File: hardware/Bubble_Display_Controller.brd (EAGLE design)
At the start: 38.1 x 43.2 mm, 37 parts, among them J1 ICSP, Q1 BSS84, Q10 BSS123, Q11 BSS123, Q12 BSS123, Q13 BSS123, Q14 BSS123, Q15 BSS123, Q16 BSS123, Q2 BSS84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

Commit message: Updating comp values per simulation. Added BOM. Started firmware.
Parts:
- C1: value 0.1u -> 0.1uF
- C3: value CAP_POL0805 -> 10uF
- Q10, Q11, Q12, Q13, Q14, Q15, Q16, Q9: value BSS123 -> IRFML8244
- R1, R2, R3, R4, R5, R6, R7, R8: value 180 -> 75
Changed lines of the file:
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@@
 <element name="DISPLAY2" library="SparkFun-Displays" package="DIL12" value="hp" x="11.43" y="29.21" rot="MR0"/>
 <element name="Q1" library="SparkFun-DiscreteSemi" package="SOT23-3" value="BSS84" x="33.02" y="39.37" rot="R180"/>
-<element name="R1" library="SparkFun-Resistors" package="0805" value="180" x="33.02" y="35.56"/>
+<element name="R1" library="SparkFun-Resistors" package="0805" value="75" x="33.02" y="35.56"/>
 <element name="Q2" library="SparkFun-DiscreteSemi" package="SOT23-3" value="BSS84" x="16.51" y="39.37" rot="R180"/>
-<element name="R2" library="SparkFun-Resistors" package="0805" value="180" x="15.24" y="35.56"/>
+<element name="R2" library="SparkFun-Resistors" package="0805" value="75" x="15.24" y="35.56"/>
 <element name="Q3" library="SparkFun-DiscreteSemi" package="SOT23-3" value="BSS84" x="30.48" y="19.05"/>
-<element name="R3" library="SparkFun-Resistors" package="0805" value="180" x="30.48" y="22.86"/>
+<element name="R3" library="SparkFun-Resistors" package="0805" value="75" x="30.48" y="22.86"/>
 <element name="Q4" library="SparkFun-DiscreteSemi" package="SOT23-3" value="BSS84" x="22.86" y="39.37" rot="R180"/>
-<element name="R4" library="SparkFun-Resistors" package="0805" value="180" x="22.86" y="35.56"/>
+<element name="R4" library="SparkFun-Resistors" package="0805" value="75" x="22.86" y="35.56"/>
 <element name="Q5" library="SparkFun-DiscreteSemi" package="SOT23-3" value="BSS84" x="15.24" y="19.05"/>
-<element name="R5" library="SparkFun-Resistors" package="0805" value="180" x="15.24" y="22.86"/>
+<element name="R5" library="SparkFun-Resistors" package="0805" value="75" x="15.24" y="22.86"/>
 <element name="Q6" library="SparkFun-DiscreteSemi" package="SOT23-3" value="BSS84" x="8.89" y="39.37" rot="R180"/>
-<element name="R6" library="SparkFun-Resistors" package="0805" value="180" x="10.16" y="35.56" rot="R180"/>
+<element name="R6" library="SparkFun-Resistors" package="0805" value="75" x="10.16" y="35.56" rot="R180"/>
 <element name="Q7" library="SparkFun-DiscreteSemi" package="SOT23-3" value="BSS84" x="5.08" y="39.37" rot="R180"/>
-<element name="R7" library="SparkFun-Resistors" package="0805" value="180" x="5.08" y="35.56"/>
+<element name="R7" library="SparkFun-Resistors" package="0805" value="75" x="5.08" y="35.56"/>
 <element name="Q8" library="SparkFun-DiscreteSemi" package="SOT23-3" value="BSS84" x="7.62" y="19.05"/>
-<element name="R8" library="SparkFun-Resistors" package="0805" value="180" x="7.62" y="22.86"/>
-<element name="C3" library="ChipsParts" package="0805-POL" value="CAP_POL0805" x="5.08" y="6.985" rot="R270"/>
-<element name="C1" library="SparkFun-Capacitors" package="0805" value="0.1u" x="16.51" y="1.905" rot="R180"/>
+<element name="R8" library="SparkFun-Resistors" package="0805" value="75" x="7.62" y="22.86"/>
+<element name="C3" library="ChipsParts" package="0805-POL" value="10uF" x="5.08" y="6.985" rot="R270"/>
+<element name="C1" library="SparkFun-Capacitors" package="0805" value="0.1uF" x="16.51" y="1.905" rot="R180"/>
 <element name="J1" library="SparkFun" package="2X3" value="ICSP" x="36.195" y="3.175" rot="R90"/>
 <element name="C5" library="SparkFun-Capacitors" package="0805" value="0.1uF" x="20.955" y="1.905"/>
@@
 <element name="Y1" library="SparkFun-FreqCtrl" package="RESONATOR-SMD" value="16MHz" x="16.51" y="15.24" rot="R180"/>
 <element name="JP1" library="SparkFun-Connectors" package="1X04" value="I2C" x="1.905" y="2.54"/>
-<element name="Q9" library="SparkFun-DiscreteSemi" package="SOT23" value="BSS123" x="34.29" y="21.59">
+<element name="Q9" library="SparkFun-DiscreteSemi" package="SOT23" value="IRFML8244" x="34.29" y="21.59">
 <attribute name="PROD_ID" value="TRANS-08345" x="69.85" y="-16.51" size="1.778" layer="27" display="off"/>
 </element>
-<element name="Q10" library="SparkFun-DiscreteSemi" package="SOT23" value="BSS123" x="27.94" y="38.1" rot="R180">
+<element name="Q10" library="SparkFun-DiscreteSemi" package="SOT23" value="IRFML8244" x="27.94" y="38.1" rot="R180">
 <attribute name="PROD_ID" value="TRANS-08345" x="-11.43" y="76.2" size="1.778" layer="27" rot="R180" display="off"/>
 </element>
-<element name="Q11" library="SparkFun-DiscreteSemi" package="SOT23" value="BSS123" x="26.67" y="21.59">
+<element name="Q11" library="SparkFun-DiscreteSemi" package="SOT23" value="IRFML8244" x="26.67" y="21.59">
 <attribute name="PROD_ID" value="TRANS-08345" x="69.85" y="-16.51" size="1.778" layer="27" display="off"/>
 </element>
-<element name="Q12" library="SparkFun-DiscreteSemi" package="SOT23" value="BSS123" x="22.86" y="21.59">
+<element name="Q12" library="SparkFun-DiscreteSemi" package="SOT23" value="IRFML8244" x="22.86" y="21.59">
 <attribute name="PROD_ID" value="TRANS-08345" x="69.85" y="-16.51" size="1.778" layer="27" display="off"/>
 </element>
-<element name="Q13" library="SparkFun-DiscreteSemi" package="SOT23" value="BSS123" x="3.81" y="21.59">
+<element name="Q13" library="SparkFun-DiscreteSemi" package="SOT23" value="IRFML8244" x="3.81" y="21.59">
 <attribute name="PROD_ID" value="TRANS-08345" x="54.61" y="-16.51" size="1.778" layer="27" display="off"/>
 </element>
-<element name="Q14" library="SparkFun-DiscreteSemi" package="SOT23" value="BSS123" x="11.43" y="21.59">
+<element name="Q14" library="SparkFun-DiscreteSemi" package="SOT23" value="IRFML8244" x="11.43" y="21.59">
 <attribute name="PROD_ID" value="TRANS-08345" x="66.04" y="-16.51" size="1.778" layer="27" display="off"/>
 </element>
-<element name="Q15" library="SparkFun-DiscreteSemi" package="SOT23" value="BSS123" x="12.7" y="38.1" rot="R180">
+<element name="Q15" library="SparkFun-DiscreteSemi" package="SOT23" value="IRFML8244" x="12.7" y="38.1" rot="R180">
 <attribute name="PROD_ID" value="TRANS-08345" x="-2.54" y="87.63" size="1.778" layer="27" rot="R180" display="off"/>
 </element>
-<element name="Q16" library="SparkFun-DiscreteSemi" package="SOT23" value="BSS123" x="19.05" y="21.59">
+<element name="Q16" library="SparkFun-DiscreteSemi" package="SOT23" value="IRFML8244" x="19.05" y="21.59">
 <attribute name="PROD_ID" value="TRANS-08345" x="38.1" y="-27.94" size="1.778" layer="27" display="off"/>
 </element>

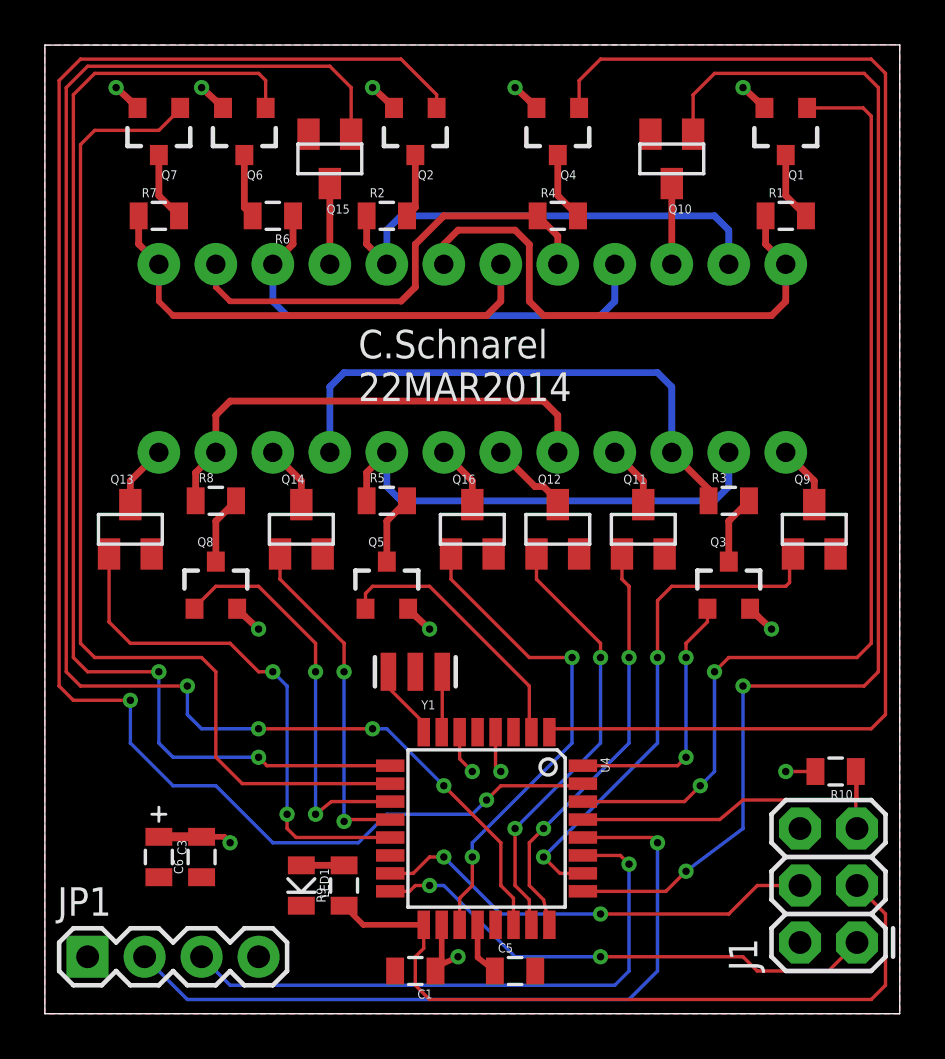
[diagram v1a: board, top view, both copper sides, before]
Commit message: Updated to use new HP Display component in my fork of SparkFun libraries
Also worked on CharGenROM.h; converted segments to HP config.  Added
proper port manipulation to Display_Firmware.ino.
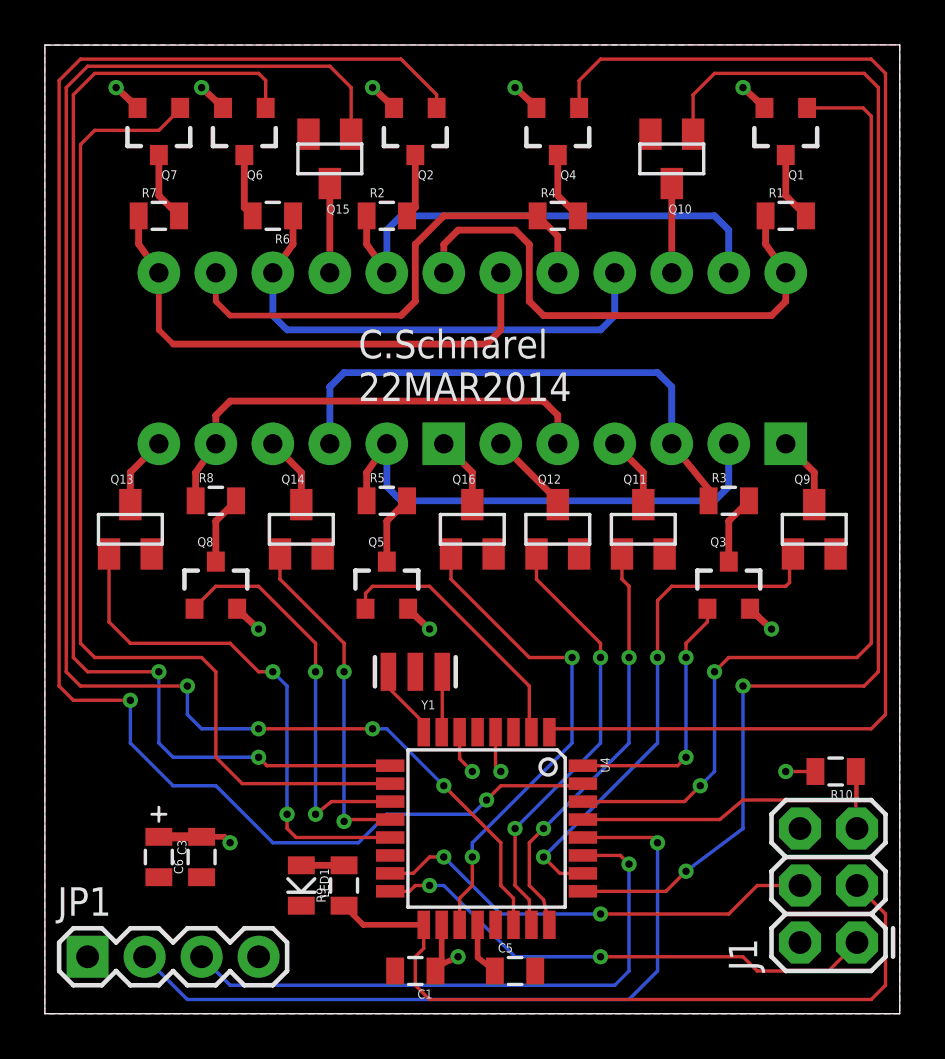
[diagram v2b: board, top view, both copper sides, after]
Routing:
- net SEGG: track 21.6 -> 23.7 mm
- net SEGD: track 20.8 -> 22.1 mm
- net SEGE: track 21.3 -> 22.4 mm
- net SEGB: track 21.3 -> 22.4 mm
- net SEGF: track 21.6 -> 22.4 mm

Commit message: Some signal name changes
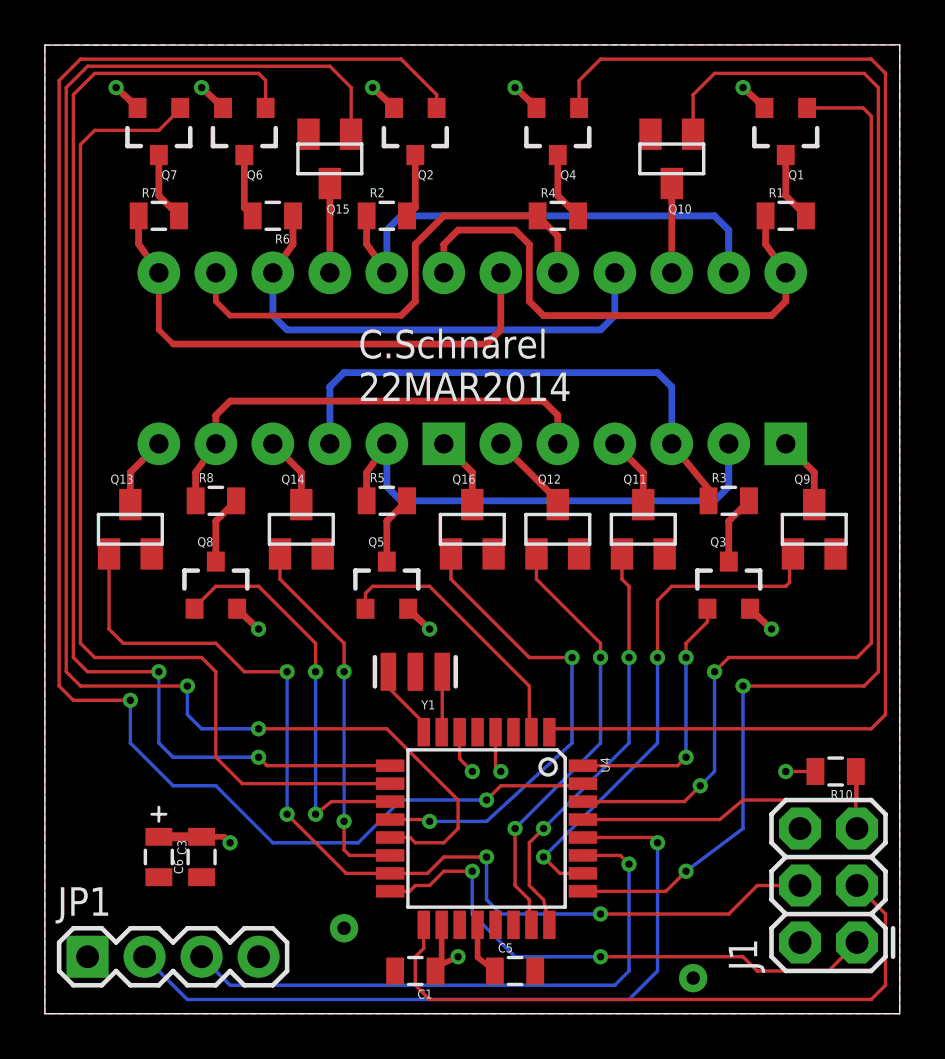
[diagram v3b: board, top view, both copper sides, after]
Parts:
- removed LED1: BLUE, ChipsParts:0805-LED
- removed R9: 1k, SparkFun-Resistors:0805
- added JP2, JP3: BREADBD_VIA, ChipsParts:BBD-VIA
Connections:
- removed net DIG8: Q13.1, U4.13
- removed net MOSI: J1.4, U4.15
- removed net N$2: LED1.A, R9.2
- removed net SS: U4.14
- new net EE1: JP2.P$1, U4.19
- new net EE2: JP3.P$1, U4.22
- new net MOSI/DIG8: J1.4, Q13.1, U4.15
- net DIG1: now also Q9.1, U4.26; no longer Q12.1, U4.23
- net DIG2: now also Q10.1, U4.25; no longer Q11.1, U4.24
- net DIG3: now also Q11.1, U4.24; no longer Q10.1, U4.25
- net DIG4: now also Q12.1, U4.23; no longer Q9.1, U4.26
- net DIG5: now also U4.12; no longer U4.19
- net DIG6: now also U4.13; no longer U4.22
- net DIG7: now also U4.14; no longer U4.12
- net GND: no longer LED1.C
- net SCK: no longer R9.1
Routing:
- net MOSI/DIG8: track 0.00 -> 45.4 mm, vias 0 -> 4
- net DIG3: track 57.5 -> 18.8 mm
- net DIG2: track 18.8 -> 57.5 mm
- net DIG8: track 23.3 -> 0.00 mm, vias 2 -> 0
- net MOSI: track 20.1 -> 0.00 mm, vias 2 -> 0
- net SCK: track 33.2 -> 29.3 mm
- net DIG4: track 23.2 -> 19.6 mm
- net DIG1: track 19.6 -> 23.2 mm
- net DIG6: track 68.8 -> 66.8 mm, vias 4 -> 2
- net N$2: track 1.91 -> 0.00 mm
- net MISO: track 23.0 -> 24.7 mm
- net DIG7: track 15.2 -> 16.5 mm
- net DIG5: track 22.0 -> 21.2 mm

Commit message: New version fixing display component bugs
Changed to correct package definition for display.
Added mounting holes.
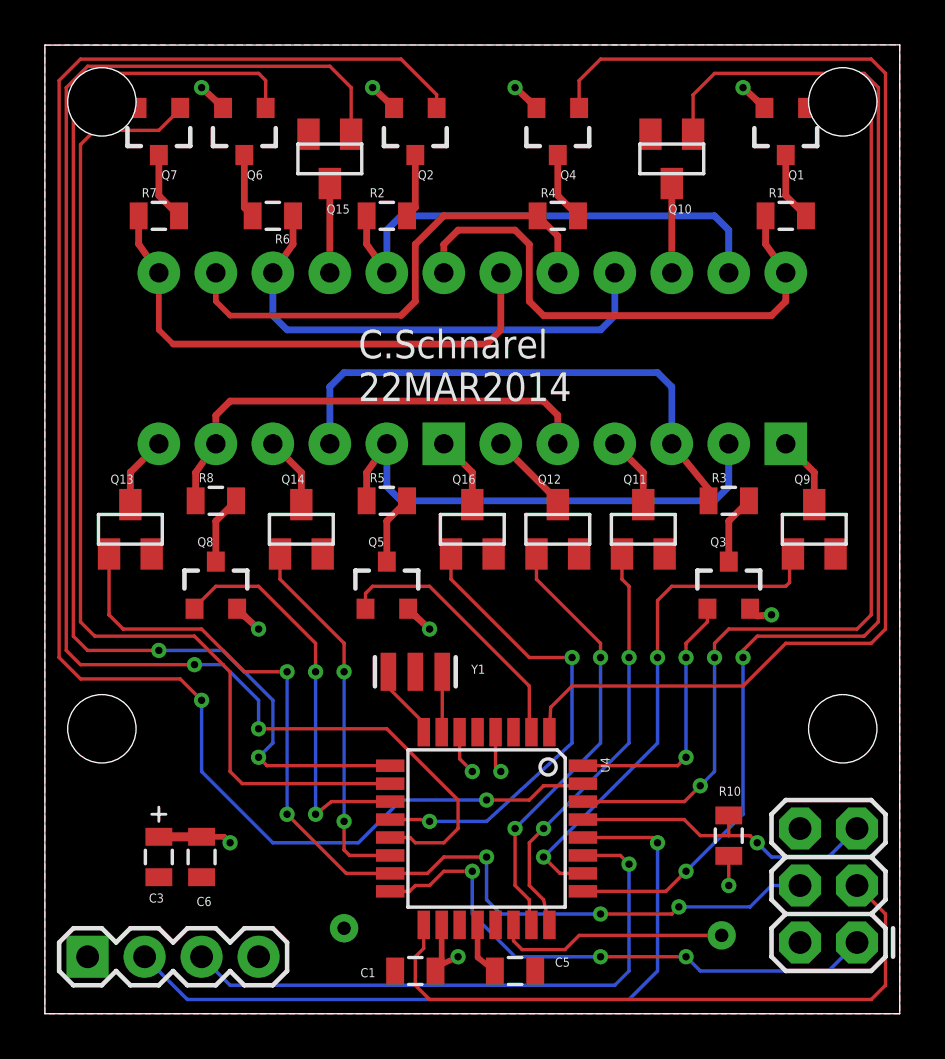
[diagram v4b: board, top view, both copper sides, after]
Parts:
- added U$5, U$6, U$7, U$8: (no value), SparkFun-Electromechanical:STAND-OFF-TIGHT
- moved R10 5.55 mm to (30.5, 7.94), turned to 270 degrees
- moved JP3 2.29 mm to (30.2, 3.49)
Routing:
- net EE2: track 0.00 -> 10.4 mm
- net RESET: track 16.5 -> 14.3 mm, vias 0 -> 1
- net D: track 59.4 -> 57.8 mm
- net DIG2: track 57.5 -> 56.9 mm
- net DIG6: track 66.8 -> 66.3 mm
- net MOSI/DIG8: track 45.4 -> 45.0 mm, vias 4 -> 5
- net MISO: vias 2 -> 3

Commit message: New HW version started. Bringing FW forward.
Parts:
- removed Q1, Q2, Q3, Q4, Q5, Q6, Q7, Q8: BSS84, SparkFun-DiscreteSemi:SOT23-3
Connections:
- removed net N$23: Q5.3, R5.2
- removed net N$25: Q1.3, R1.2
- removed net N$27: Q6.3, R6.2
- removed net N$28: Q2.3, R2.2
- removed net N$30: Q3.3, R3.2
- removed net N$32: Q4.3, R4.2
- removed net N$33: Q7.3, R7.2
- removed net N$34: Q8.3, R8.2
- net 5V: no longer Q1.2, Q2.2, Q3.2, Q4.2, Q5.2, Q6.2, Q7.2, Q8.2
- net A: now also R1.2; no longer Q1.1
- net B: now also R2.2; no longer Q2.1
- net C: now also R3.2; no longer Q3.1
- net D: now also R4.2; no longer Q4.1
- net DP: now also R8.2; no longer Q8.1
- net E: now also R5.2; no longer Q5.1
- net F: now also R6.2; no longer Q6.1
- net G: now also R7.2; no longer Q7.1
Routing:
- net 5V: track 22.1 -> 11.8 mm, vias 13 -> 5
- net A: track 44.9 -> 38.4 mm
- net DIG2: track 56.9 -> 51.1 mm
- net N$32: track 3.08 -> 0.00 mm
- net N$33: track 3.08 -> 0.00 mm
- net N$23: track 3.08 -> 0.00 mm
- net N$34: track 3.08 -> 0.00 mm
- net N$30: track 3.08 -> 0.00 mm
- net N$25: track 3.08 -> 0.00 mm
- net N$28: track 2.86 -> 0.00 mm
- net N$27: track 2.86 -> 0.00 mm
- net D: track 57.8 -> 56.5 mm
- net G: track 45.8 -> 47.0 mm
- net DP: track 18.0 -> 19.3 mm
- net F: track 53.3 -> 52.6 mm
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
